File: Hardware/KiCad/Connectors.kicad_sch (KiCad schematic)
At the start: 57 parts

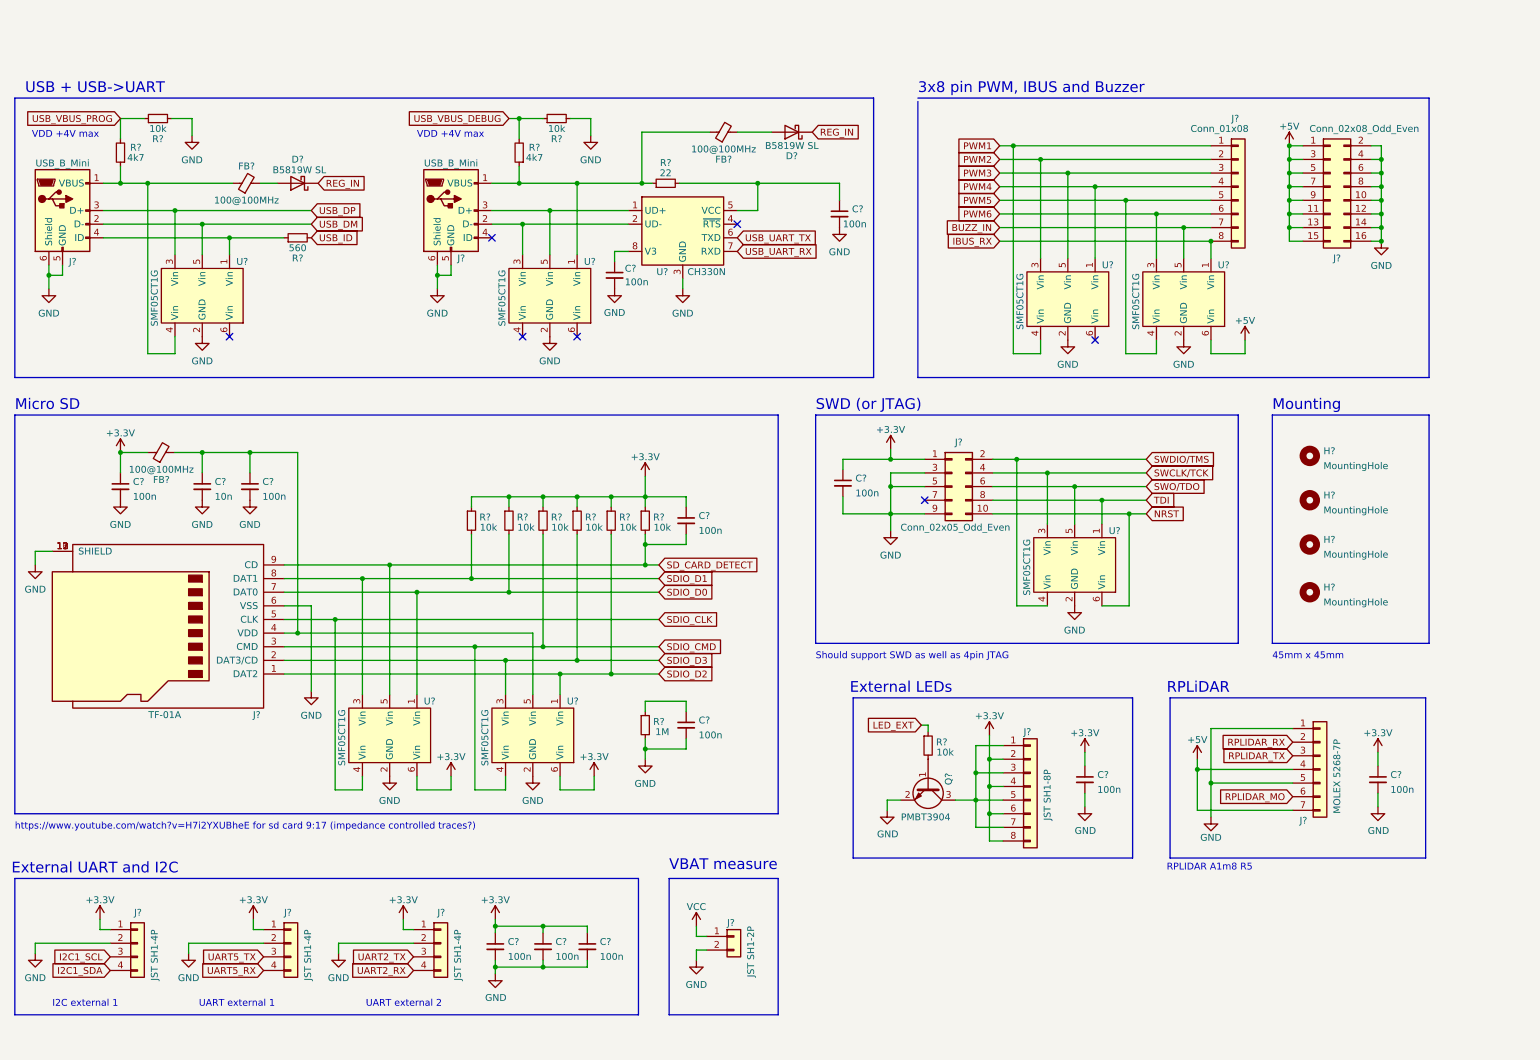
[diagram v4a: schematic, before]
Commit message: Added more current limiting resistors
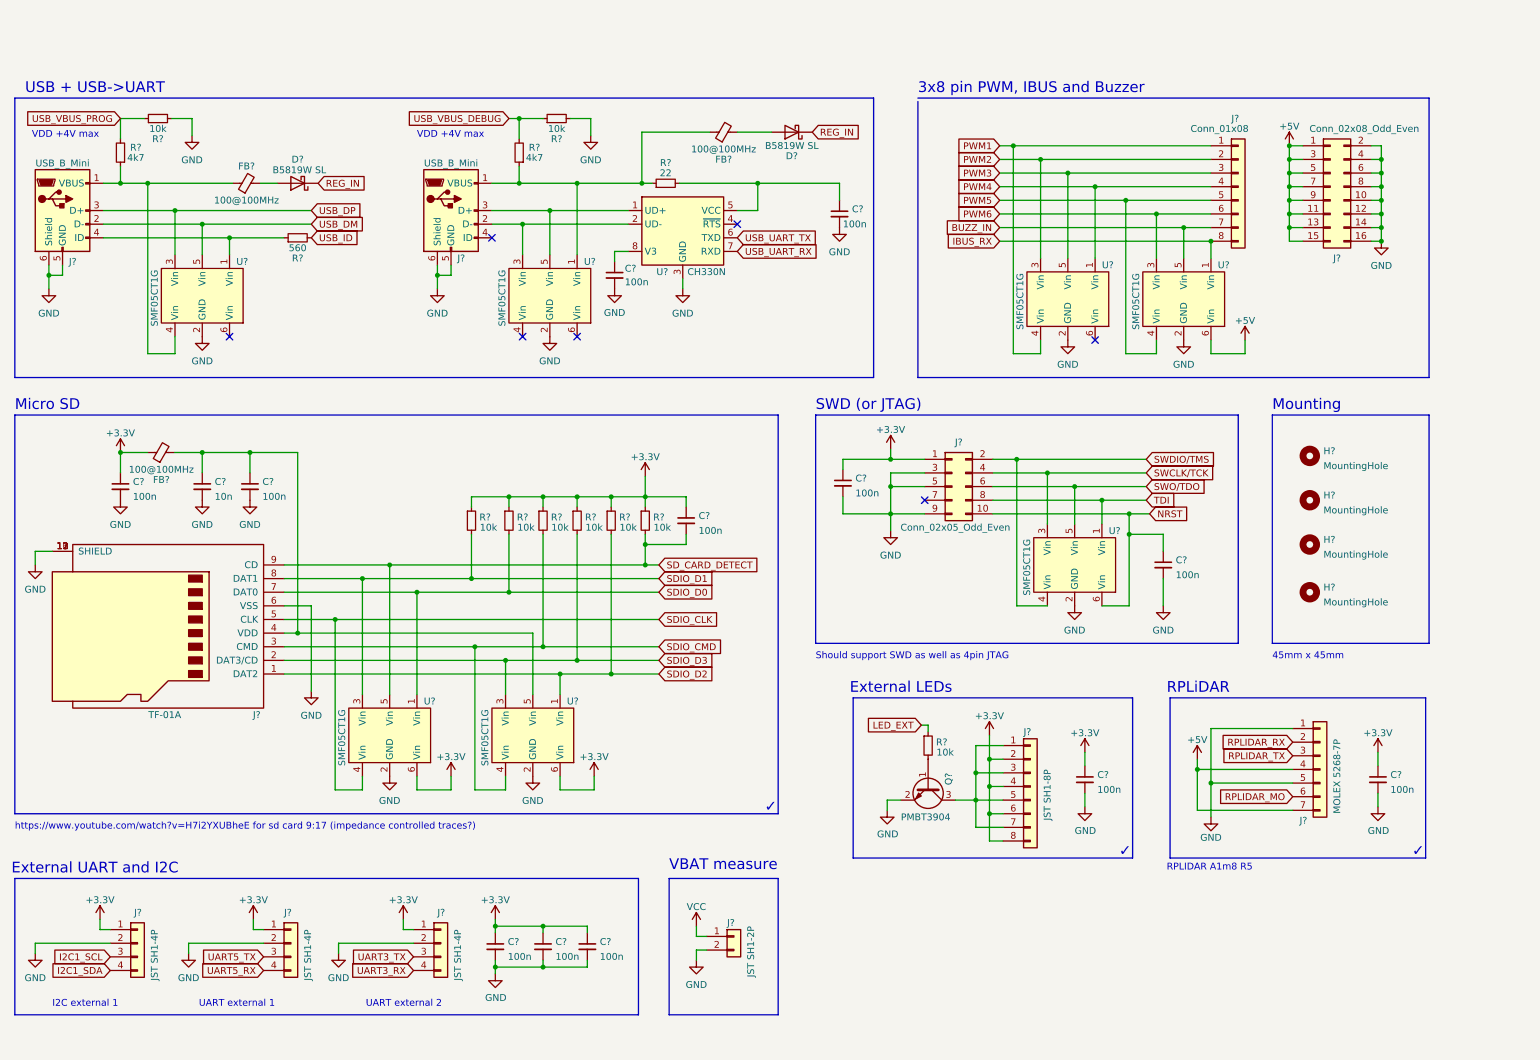
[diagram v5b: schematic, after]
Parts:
- removed C?: 100n, Capacitor_SMD:C_0402_1005Metric, symbol Device:C_Small
- removed R?: 1M, Resistor_SMD:R_0402_1005Metric, symbol Device:R_Small
- added C?: 100n, Capacitor_SMD:C_0402_1005Metric, symbol Device:C_Small
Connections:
- net GND: now also C?.2
- net NRST: now also C?.1
- net UART2_RX renamed UART3_RX
- net UART2_TX renamed UART3_TX
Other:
- note added: "✓"
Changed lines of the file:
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@@
   (junction (at 252.095 43.18) (diameter 0) (color 0 0 0 0)
   )
-  (junction (at 132.08 140.335) (diameter 0) (color 0 0 0 0)
-  )
   (junction (at 269.24 33.02) (diameter 0) (color 0 0 0 0)
   )
@@
   )
   (junction (at 125.73 126.365) (diameter 0) (color 0 0 0 0)
+  )
+  (junction (at 222.25 100.33) (diameter 0) (color 0 0 0 0)
   )
   (junction (at 104.14 173.355) (diameter 0) (color 0 0 0 0)
@@
     (stroke (width 0) (type default) (color 0 0 0 0))
   )
+  (wire (pts (xy 228.6 100.33) (xy 222.25 100.33))
+    (stroke (width 0) (type default) (color 0 0 0 0))
+  )
   (wire (pts (xy 132.08 102.235) (xy 132.08 106.045))
     (stroke (width 0) (type default) (color 0 0 0 0))
@@
     (stroke (width 0) (type default) (color 0 0 0 0))
   )
+  (wire (pts (xy 228.6 103.505) (xy 228.6 100.33))
+    (stroke (width 0) (type default) (color 0 0 0 0))
+  )
   (wire (pts (xy 237.49 136.525) (xy 237.49 146.685))
     (stroke (width 0) (type default) (color 0 0 0 0))
@@
     (stroke (width 0) (type default) (color 0 0 0 0))
   )
+  (wire (pts (xy 228.6 108.585) (xy 228.6 113.665))
+    (stroke (width 0) (type default) (color 0 0 0 0))
+  )
   (wire (pts (xy 31.115 40.005) (xy 44.45 40.005))
     (stroke (width 0) (type default) (color 0 0 0 0))
@@
     (stroke (width 0) (type default) (color 0 0 0 0))
   )
-  (wire (pts (xy 139.7 131.445) (xy 132.08 131.445))
-    (stroke (width 0) (type default) (color 0 0 0 0))
-  )
-  (wire (pts (xy 222.25 96.52) (xy 222.25 113.665))
+  (wire (pts (xy 222.25 96.52) (xy 222.25 100.33))
     (stroke (width 0) (type default) (color 0 0 0 0))
   )
@@
     (stroke (width 0) (type default) (color 0 0 0 0))
   )
-  (wire (pts (xy 132.08 140.335) (xy 132.08 138.43))
-    (stroke (width 0) (type default) (color 0 0 0 0))
-  )
   (wire (pts (xy 121.285 173.355) (xy 121.285 174.625))
     (stroke (width 0) (type default) (color 0 0 0 0))
@@
     (stroke (width 0) (type default) (color 0 0 0 0))
   )
-  (wire (pts (xy 132.08 131.445) (xy 132.08 133.35))
-    (stroke (width 0) (type default) (color 0 0 0 0))
-  )
   (wire (pts (xy 193.675 149.86) (xy 193.675 154.94))
     (stroke (width 0) (type default) (color 0 0 0 0))
@@
     (stroke (width 0) (type default) (color 0 0 0 0))
   )
-  (wire (pts (xy 139.7 133.35) (xy 139.7 131.445))
-    (stroke (width 0) (type default) (color 0 0 0 0))
-  )
   (wire (pts (xy 234.95 144.145) (xy 252.73 144.145))
     (stroke (width 0) (type default) (color 0 0 0 0))
@@
     (stroke (width 0) (type default) (color 0 0 0 0))
   )
-  (wire (pts (xy 139.7 138.43) (xy 139.7 140.335))
-    (stroke (width 0) (type default) (color 0 0 0 0))
-  )
-  (wire (pts (xy 132.08 140.335) (xy 132.08 142.24))
-    (stroke (width 0) (type default) (color 0 0 0 0))
-  )
   (wire (pts (xy 74.295 147.955) (xy 79.375 147.955))
     (stroke (width 0) (type default) (color 0 0 0 0))
@@
     (stroke (width 0) (type default) (color 0 0 0 0))
   )
-  (wire (pts (xy 222.25 96.52) (xy 225.425 96.52))
-    (stroke (width 0) (type default) (color 0 0 0 0))
-  )
   (wire (pts (xy 108.585 34.925) (xy 108.585 31.75))
     (stroke (width 0) (type default) (color 0 0 0 0))
@@
     (stroke (width 0) (type default) (color 0 0 0 0))
   )
+  (wire (pts (xy 222.25 100.33) (xy 222.25 113.665))
+    (stroke (width 0) (type default) (color 0 0 0 0))
+  )
   (wire (pts (xy 114.3 40.005) (xy 128.905 40.005))
     (stroke (width 0) (type default) (color 0 0 0 0))
@@
     (stroke (width 0) (type default) (color 0 0 0 0))
   )
+  (wire (pts (xy 222.25 96.52) (xy 226.06 96.52))
+    (stroke (width 0) (type default) (color 0 0 0 0))
+  )
   (wire (pts (xy 267.335 38.1) (xy 269.24 38.1))
     (stroke (width 0) (type default) (color 0 0 0 0))
@@
   )
   (wire (pts (xy 119.38 123.825) (xy 134.62 123.825))
-    (stroke (width 0) (type default) (color 0 0 0 0))
-  )
-  (wire (pts (xy 139.7 140.335) (xy 132.08 140.335))
     (stroke (width 0) (type default) (color 0 0 0 0))
   )
@@
     (effects (font (size 2 2)) (justify left bottom))
   )
+  (text "✓" (at 220.345 160.655 0)
+    (effects (font (size 2 2)) (justify left bottom))
+  )
   (text "Micro SD" (at 14.605 77.47 0)
     (effects (font (size 2 2)) (justify left bottom))
@@
     (effects (font (size 1.27 1.27)) (justify left bottom))
   )
+  (text "✓" (at 154.305 152.4 0)
+    (effects (font (size 2 2)) (justify left bottom))
+  )
   (text "RPLIDAR A1m8 R5" (at 229.235 163.195 0)
     (effects (font (size 1.27 1.27)) (justify left bottom))
@@
   )
   (text "SWD (or JTAG)" (at 163.83 77.47 0)
+    (effects (font (size 2 2)) (justify left bottom))
+  )
+  (text "✓" (at 274.955 160.655 0)
     (effects (font (size 2 2)) (justify left bottom))
   )
@@
     )
   )
-  (global_label "UART2_RX" (shape input) (at 88.9 181.61 180) (fields_autoplaced)
+  (global_label "UART3_RX" (shape input) (at 88.9 181.61 180) (fields_autoplaced)
     (effects (font (size 1.27 1.27)) (justify right))
     (property "Intersheet References" "${INTERSHEET_REFS}" (id 0) (at 77.1736 181.5306 0)
@@
     )
   )
-  (global_label "NRST" (shape input) (at 225.425 96.52 0) (fields_autoplaced)
+  (global_label "NRST" (shape input) (at 226.06 96.52 0) (fields_autoplaced)
     (effects (font (size 1.27 1.27)) (justify left))
-    (property "Intersheet References" "${INTERSHEET_REFS}" (id 0) (at 232.6157 96.4406 0)
+    (property "Intersheet References" "${INTERSHEET_REFS}" (id 0) (at 233.2507 96.4406 0)
       (effects (font (size 1.27 1.27)) (justify left) hide)
     )
@@
     )
   )
-  (global_label "UART2_TX" (shape input) (at 88.9 179.07 180) (fields_autoplaced)
+  (global_label "UART3_TX" (shape input) (at 88.9 179.07 180) (fields_autoplaced)
     (effects (font (size 1.27 1.27)) (justify right))
     (property "Intersheet References" "${INTERSHEET_REFS}" (id 0) (at 77.4759 178.9906 0)
@@
     (pin "1")
   )
-  (symbol (lib_id "Device:R_Small") (at 132.08 135.89 0) (unit 1)
-    (in_bom yes) (on_board yes)
-    (property "Reference" "R?" (id 0) (at 134.62 135.255 0))
-    (property "Value" "1M" (id 1) (at 135.255 137.16 0))
-    (property "Footprint" "Resistor_SMD:R_0402_1005Metric" (id 2) (at 132.08 135.89 0)
-      (effects (font (size 1.27 1.27)) hide)
-    )
-    (property "Datasheet" "~" (id 3) (at 132.08 135.89 0)
-      (effects (font (size 1.27 1.27)) hide)
-    )
-    (pin "1")
-    (pin "2")
-  )
   (symbol (lib_id "Device:R_Small") (at 108.585 29.21 180) (unit 1)
     (in_bom yes) (on_board yes)
@@
     (pin "5")
     (pin "6")
+  )
+  (symbol (lib_id "power:GND") (at 228.6 113.665 0) (unit 1)
+    (in_bom yes) (on_board yes) (fields_autoplaced)
+    (property "Reference" "#PWR?" (id 0) (at 228.6 120.015 0)
+      (effects (font (size 1.27 1.27)) hide)
+    )
+    (property "Value" "GND" (id 1) (at 228.6 118.2275 0))
+    (property "Footprint" "" (id 2) (at 228.6 113.665 0)
+      (effects (font (size 1.27 1.27)) hide)
+    )
+    (property "Datasheet" "" (id 3) (at 228.6 113.665 0)
+      (effects (font (size 1.27 1.27)) hide)
+    )
+    (pin "1")
   )
   (symbol (lib_id "Device:R_Small") (at 119.38 97.79 0) (unit 1)
@@
     (pin "1")
   )
-  (symbol (lib_id "power:GND") (at 132.08 142.24 0) (unit 1)
-    (in_bom yes) (on_board yes) (fields_autoplaced)
-    (property "Reference" "#PWR0147" (id 0) (at 132.08 148.59 0)
-      (effects (font (size 1.27 1.27)) hide)
-    )
-    (property "Value" "GND" (id 1) (at 132.08 146.8025 0))
-    (property "Footprint" "" (id 2) (at 132.08 142.24 0)
-      (effects (font (size 1.27 1.27)) hide)
-    )
-    (property "Datasheet" "" (id 3) (at 132.08 142.24 0)
-      (effects (font (size 1.27 1.27)) hide)
-    )
-    (pin "1")
-  )
   (symbol (lib_id "Device:C_Small") (at 58.42 91.44 0) (unit 1)
     (in_bom yes) (on_board yes)
@@
     )
     (property "Datasheet" "~" (id 3) (at 49.53 91.44 0)
-      (effects (font (size 1.27 1.27)) hide)
-    )
-    (pin "1")
-    (pin "2")
-  )
-  (symbol (lib_id "Device:C_Small") (at 139.7 135.89 0) (unit 1)
-    (in_bom yes) (on_board yes) (fields_autoplaced)
-    (property "Reference" "C?" (id 0) (at 142.0241 134.9878 0)
-      (effects (font (size 1.27 1.27)) (justify left))
-    )
-    (property "Value" "100n" (id 1) (at 142.0241 137.7629 0)
-      (effects (font (size 1.27 1.27)) (justify left))
-    )
-    (property "Footprint" "Capacitor_SMD:C_0402_1005Metric" (id 2) (at 139.7 135.89 0)
-      (effects (font (size 1.27 1.27)) hide)
-    )
-    (property "Datasheet" "~" (id 3) (at 139.7 135.89 0)
       (effects (font (size 1.27 1.27)) hide)
     )
@@
     (pin "1")
   )
+  (symbol (lib_id "Device:C_Small") (at 228.6 106.045 0) (unit 1)
+    (in_bom yes) (on_board yes) (fields_autoplaced)
+    (property "Reference" "C?" (id 0) (at 230.9241 105.1428 0)
+      (effects (font (size 1.27 1.27)) (justify left))
+    )
+    (property "Value" "100n" (id 1) (at 230.9241 107.9179 0)
+      (effects (font (size 1.27 1.27)) (justify left))
+    )
+    (property "Footprint" "Capacitor_SMD:C_0402_1005Metric" (id 2) (at 228.6 106.045 0)
+      (effects (font (size 1.27 1.27)) hide)
+    )
+    (property "Datasheet" "~" (id 3) (at 228.6 106.045 0)
+      (effects (font (size 1.27 1.27)) hide)
+    )
+    (pin "1")
+    (pin "2")
+  )
   (symbol (lib_id "power:+5V") (at 252.095 27.94 0) (unit 1)
